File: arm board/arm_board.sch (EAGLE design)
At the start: 97 parts, among them IC1 OPAMP-DUALU, J1 APPPP45_PCB_HORIZ_RIGHT, J14 APPPP45_PCB_HORIZ_RIGHT, J15 APPPP45_PCB_HORIZ_RIGHT, J16 APPPP45_PCB_HORIZ_RIGHT, J17 APPPP45_PCB_HORIZ_RIGHT, J18 APPPP45_PCB_HORIZ_RIGHT, J19 ENCODER, J2 APPPP45_PCB_HORIZ_RIGHT, J20 ENCODER, J21 ENCODER, J22 ENCODER, J24 ENCODER, J3 APPPP45_PCB_HORIZ_RIGHT, Q1 Q_IRF7437SMD, U1 TIVA-1294, U3 MAX3232D

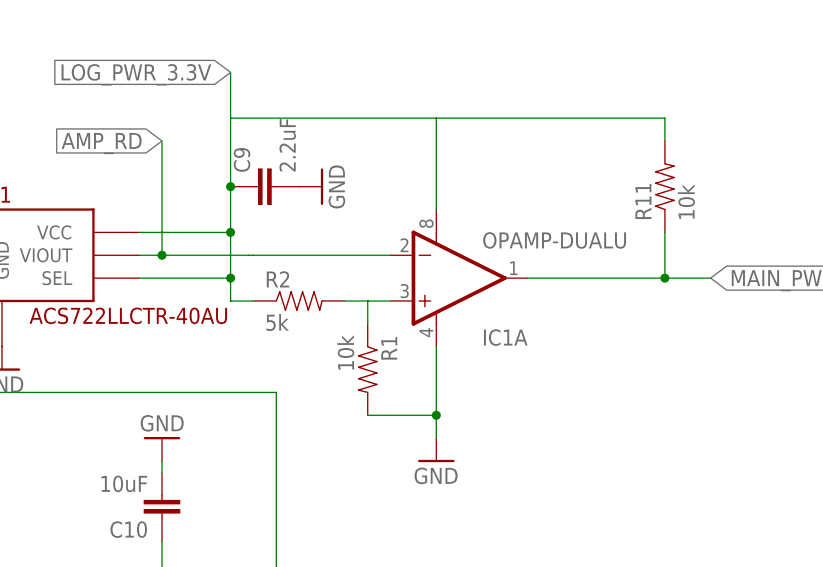
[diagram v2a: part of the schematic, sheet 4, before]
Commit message: Replaced opamp with one that actually exists
Turns out the one from sparkfun doesn't describe any model capable of
being found on digikey. wtf
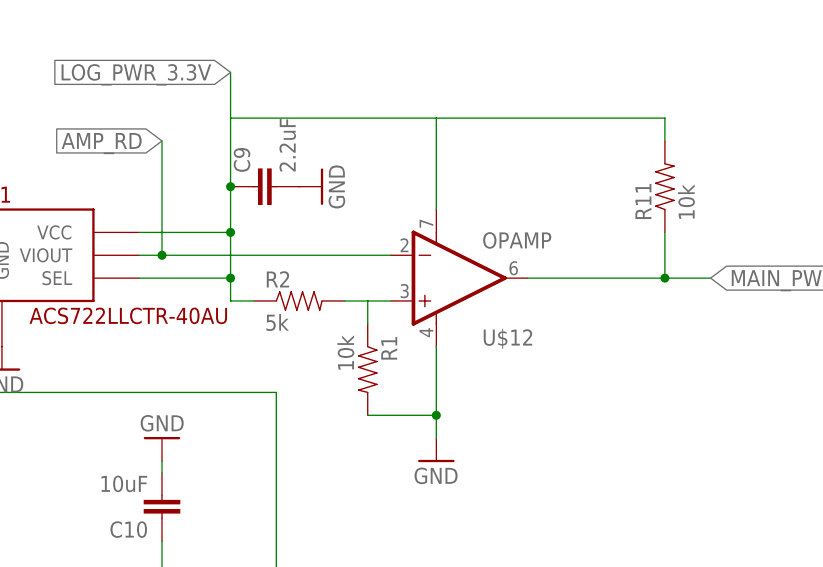
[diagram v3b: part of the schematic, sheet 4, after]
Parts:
- removed IC1: OPAMP-DUALU, SparkFun-AnalogIC:OPAMP-DUALU
- added U$12: OPAMP, MRDT-Semiconductors:OPAMP
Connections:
- net AMP_RD: now also U$12.-IN; no longer IC1A.-IN
- net GND: now also U$12.V-; no longer IC1A.V-
- net LOG_PWR_3.3V: now also U$12.V+; no longer IC1A.V+
- net MAIN_PWR_SWITCH_NFAULT: now also U$12.OUT; no longer IC1A.OUT
- net N$7: now also U$12.+IN; no longer IC1A.+IN
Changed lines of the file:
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@@
 <part name="C9" library="SparkFun-Capacitors" deviceset="0.1UF-25V(+80/-20%)(0603)" device="" value="2.2uF"/>
 <part name="GND24" library="SparkFun-Aesthetics" deviceset="GND" device=""/>
-<part name="IC1" library="SparkFun-AnalogIC" deviceset="OPAMP-DUAL" device="U"/>
 <part name="GND25" library="SparkFun-Aesthetics" deviceset="GND" device=""/>
 <part name="R1" library="SparkFun-Passives" deviceset="RESISTOR" device="0603-RES" value="10k"/>
@@
 <part name="D1" library="SparkFun-LED" deviceset="LED-YELLOW" device="LILYPAD" value="Yellow"/>
 <part name="R15" library="SparkFun-Resistors" deviceset="8.2K-5%" device="" value="3.3k"/>
+<part name="U$12" library="MRDT-Semiconductors" deviceset="OPAMP" device=""/>
 </parts>
 <sheets>
@@
 <instance part="C9" gate="G$1" x="33.02" y="-15.24" rot="R90"/>
 <instance part="GND24" gate="1" x="38.1" y="-15.24" rot="R90"/>
-<instance part="IC1" gate="A" x="50.8" y="-25.4"/>
 <instance part="GND25" gate="1" x="50.8" y="-45.72"/>
 <instance part="R1" gate="G$1" x="43.18" y="-35.56" rot="R270"/>
@@
 <instance part="GND30" gate="1" x="-129.54" y="-50.8" rot="R270"/>
 <instance part="FRAME4" gate="G$1" x="-210.82" y="-157.48"/>
+<instance part="U$12" gate="G$1" x="50.8" y="-25.4"/>
 </instances>
 <busses>
@@
 </segment>
 <segment>
-<pinref part="IC1" gate="A" pin="V-"/>
 <pinref part="GND25" gate="1" pin="GND"/>
 <wire x1="50.8" y1="-43.18" x2="50.8" y2="-40.64" width="0.1524" layer="91"/>
@@
 <wire x1="43.18" y1="-40.64" x2="50.8" y2="-40.64" width="0.1524" layer="91"/>
 <junction x="50.8" y="-40.64"/>
+<pinref part="U$12" gate="G$1" pin="V-"/>
 </segment>
 <segment>
@@
 <pinref part="C9" gate="G$1" pin="1"/>
 <junction x="27.94" y="-15.24"/>
-<pinref part="IC1" gate="A" pin="V+"/>
 <wire x1="27.94" y1="-25.4" x2="27.94" y2="-20.32" width="0.1524" layer="91"/>
 <wire x1="27.94" y1="-20.32" x2="27.94" y2="-15.24" width="0.1524" layer="91"/>
@@
 <wire x1="17.78" y1="-25.4" x2="27.94" y2="-25.4" width="0.1524" layer="91"/>
 <junction x="27.94" y="-25.4"/>
+<pinref part="U$12" gate="G$1" pin="V+"/>
 </segment>
 </net>
@@
 <junction x="20.32" y="-22.86"/>
 <label x="20.32" y="-10.16" size="1.778" layer="95" rot="R180" xref="yes"/>
-<pinref part="IC1" gate="A" pin="-IN"/>
-<wire x1="29.972" y1="-22.86" x2="30.48" y2="-22.86" width="0.1524" layer="91"/>
-<wire x1="30.48" y1="-22.86" x2="45.72" y2="-22.86" width="0.1524" layer="91"/>
-<wire x1="20.32" y1="-22.86" x2="29.972" y2="-22.86" width="0.1524" layer="91"/>
+<wire x1="20.32" y1="-22.86" x2="45.72" y2="-22.86" width="0.1524" layer="91"/>
+<pinref part="U$12" gate="G$1" pin="-IN"/>
 </segment>
 </net>
@@
 <segment>
 <pinref part="R2" gate="G$1" pin="2"/>
-<pinref part="IC1" gate="A" pin="+IN"/>
 <wire x1="40.64" y1="-27.94" x2="43.18" y2="-27.94" width="0.1524" layer="91"/>
 <pinref part="R1" gate="G$1" pin="1"/>
 <wire x1="43.18" y1="-27.94" x2="45.72" y2="-27.94" width="0.1524" layer="91"/>
 <wire x1="43.18" y1="-30.48" x2="43.18" y2="-27.94" width="0.1524" layer="91"/>
+<pinref part="U$12" gate="G$1" pin="+IN"/>
 </segment>
 </net>
 <net name="MAIN_PWR_SWITCH_NFAULT" class="0">
 <segment>
-<pinref part="IC1" gate="A" pin="OUT"/>
 <wire x1="60.96" y1="-25.4" x2="76.2" y2="-25.4" width="0.1524" layer="91"/>
 <label x="81.28" y="-25.4" size="1.778" layer="95" xref="yes"/>
@@
 <wire x1="76.2" y1="-20.32" x2="76.2" y2="-25.4" width="0.1524" layer="91"/>
 <junction x="76.2" y="-25.4"/>
-</segment>
-</net>
+<pinref part="U$12" gate="G$1" pin="OUT"/>
+</segment>
+</net>

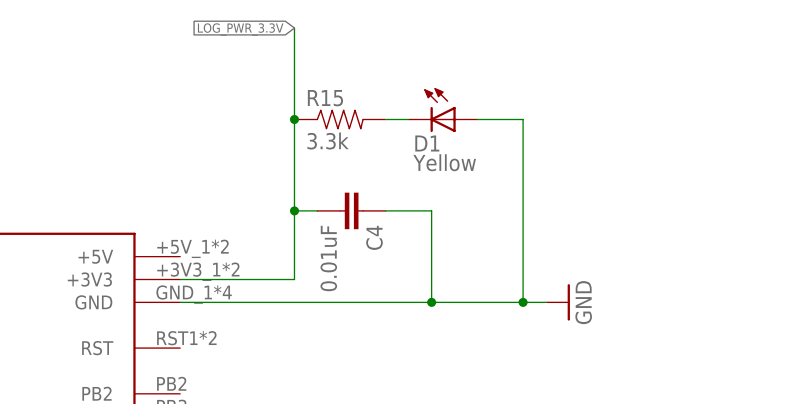
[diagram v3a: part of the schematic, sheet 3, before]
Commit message: I put the led on backwards. :-1:
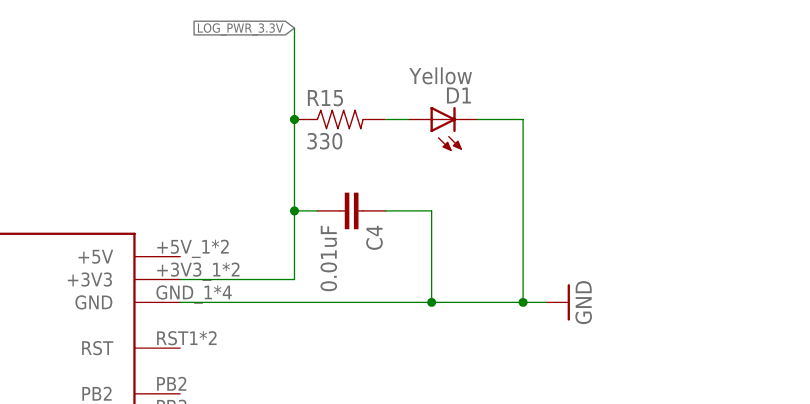
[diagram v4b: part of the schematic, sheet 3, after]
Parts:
- R15: value 3.3k -> 330
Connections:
- net GND: now also D1.C; no longer D1.A
- net N$16: now also D1.A; no longer D1.C
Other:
- moved on the sheet: D1
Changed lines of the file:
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@@
 <part name="FRAME4" library="frames" deviceset="A3L-LOC" device=""/>
 <part name="D1" library="SparkFun-LED" deviceset="LED-YELLOW" device="LILYPAD" value="Yellow"/>
-<part name="R15" library="SparkFun-Resistors" deviceset="8.2K-5%" device="" value="3.3k"/>
+<part name="R15" library="SparkFun-Resistors" deviceset="8.2K-5%" device="" value="330"/>
 <part name="U$12" library="MRDT-Semiconductors" deviceset="OPAMP" device=""/>
 </parts>
@@
 <instance part="GND15" gate="1" x="170.18" y="53.34"/>
 <instance part="FRAME3" gate="G$1" x="-99.06" y="-20.32"/>
-<instance part="D1" gate="G$1" x="53.34" y="137.16" rot="R270"/>
+<instance part="D1" gate="G$1" x="50.8" y="137.16" rot="R90"/>
 <instance part="R15" gate="G$1" x="40.64" y="137.16"/>
 </instances>
@@
 <wire x1="50.8" y1="127" x2="50.8" y2="116.84" width="0.1524" layer="91"/>
 <junction x="50.8" y="116.84"/>
-<pinref part="D1" gate="G$1" pin="A"/>
-<wire x1="55.88" y1="137.16" x2="60.96" y2="137.16" width="0.1524" layer="91"/>
 <wire x1="60.96" y1="137.16" x2="60.96" y2="116.84" width="0.1524" layer="91"/>
 <junction x="60.96" y="116.84"/>
+<pinref part="D1" gate="G$1" pin="C"/>
+<wire x1="55.88" y1="137.16" x2="60.96" y2="137.16" width="0.1524" layer="91"/>
 </segment>
 <segment>
@@
 <segment>
 <pinref part="R15" gate="G$1" pin="2"/>
-<pinref part="D1" gate="G$1" pin="C"/>
+<pinref part="D1" gate="G$1" pin="A"/>
 <wire x1="45.72" y1="137.16" x2="48.26" y2="137.16" width="0.1524" layer="91"/>
 </segment>

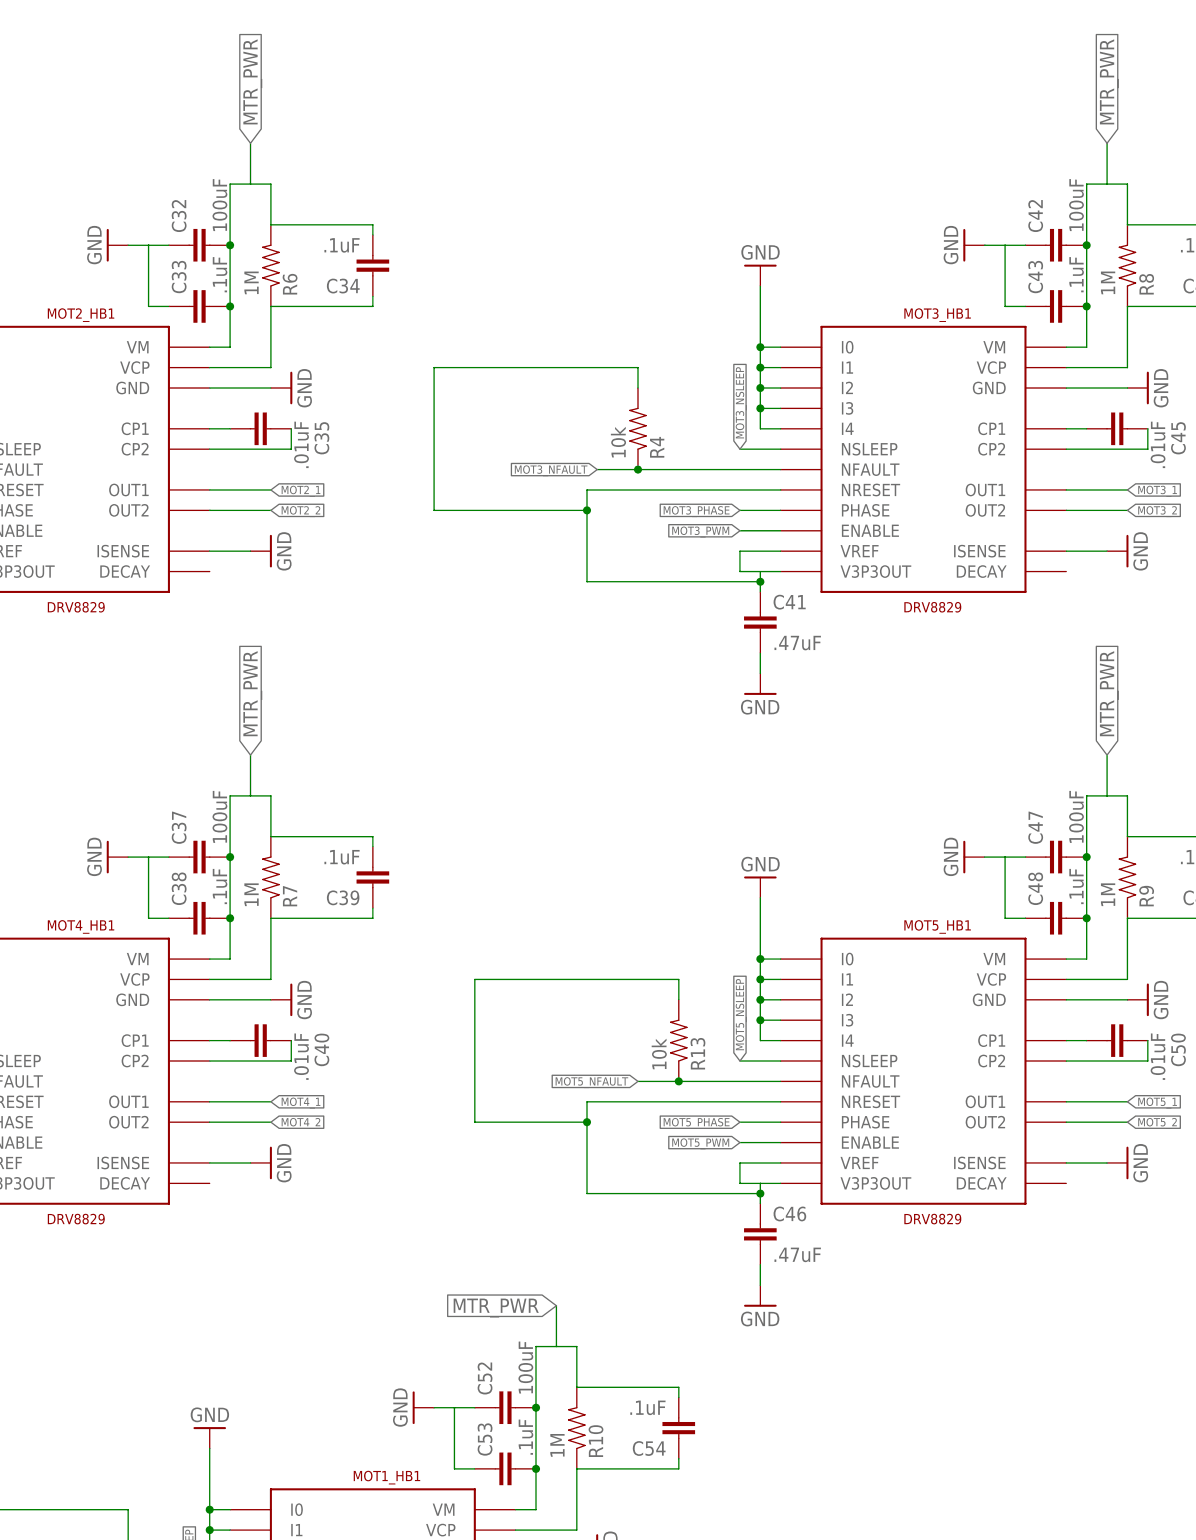
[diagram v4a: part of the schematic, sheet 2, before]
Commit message: Replaced 100uF 603 caps with 1210 caps
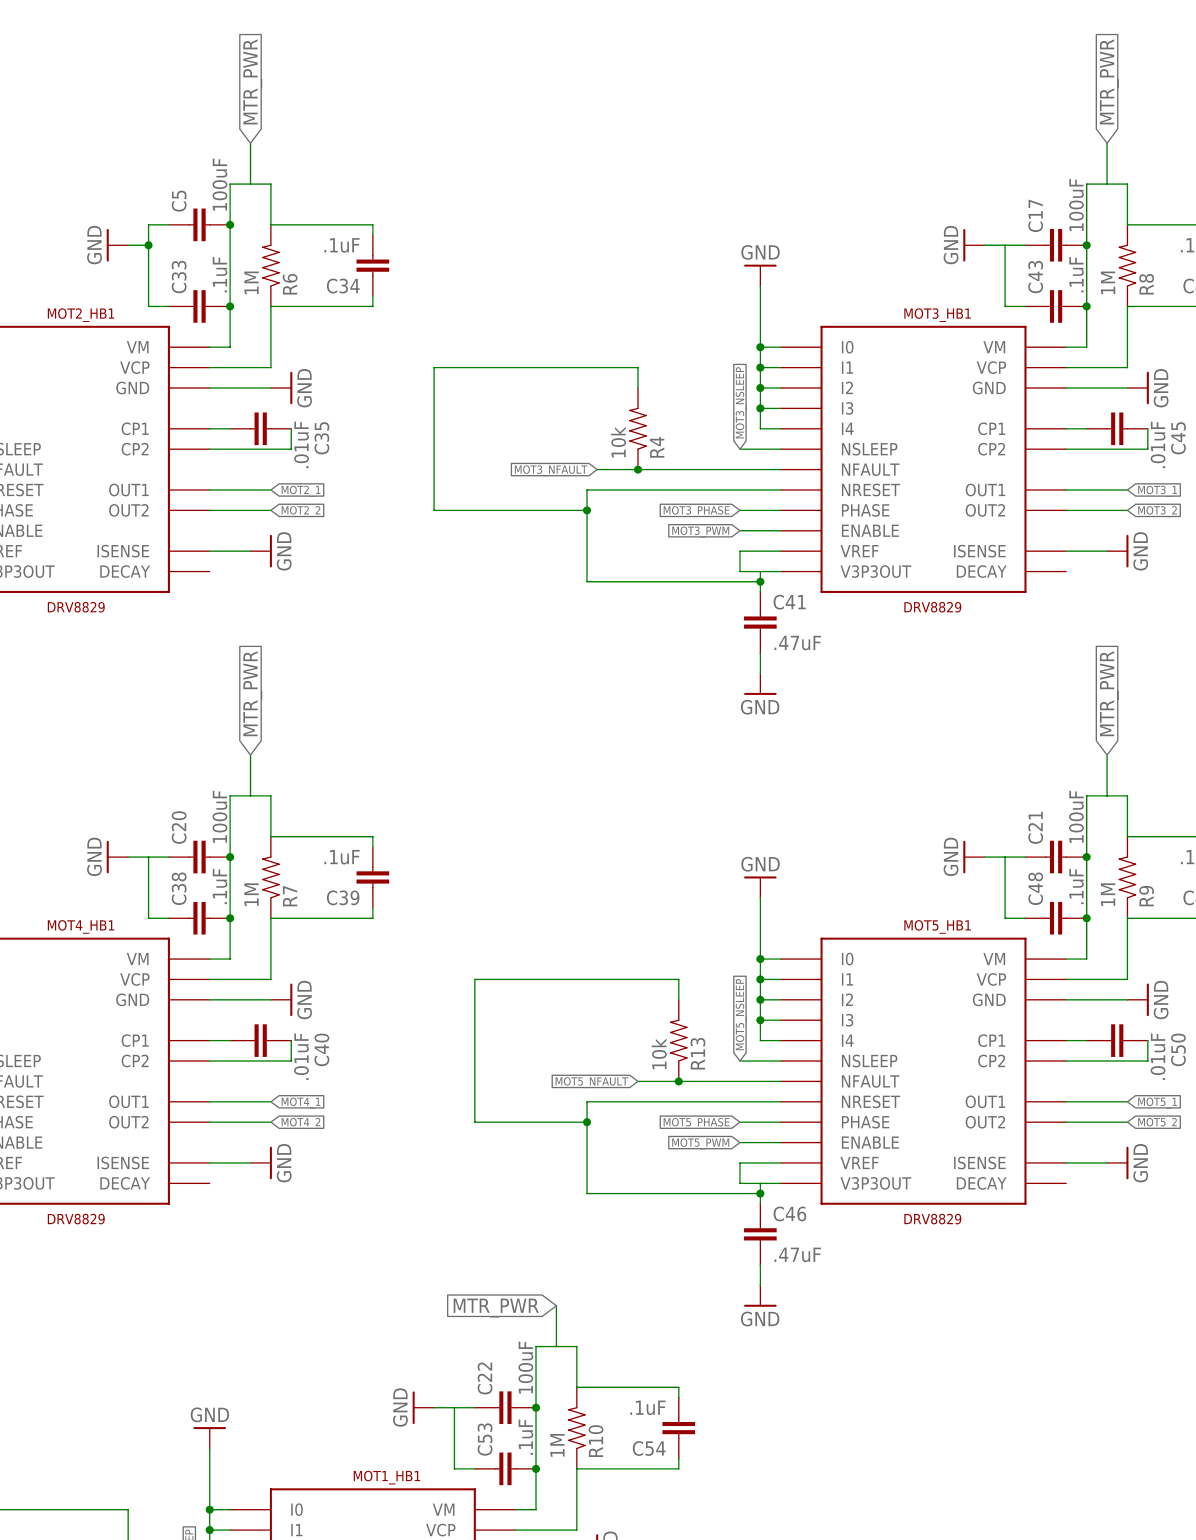
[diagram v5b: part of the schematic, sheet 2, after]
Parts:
- removed C32, C37, C42, C47, C52: 100uF, SparkFun-Capacitors:0.1UF-25V(+80/-20%)(0603)
- added C17, C20, C21, C22, C5: 100uF, SparkFun-Capacitors:CAP1210
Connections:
- net GND: now also C17.1, C20.1, C21.1, C22.1, C5.1; no longer C32.1, C37.1, C42.1, C47.1, C52.1
- net MTR_PWR: now also C17.2, C20.2, C21.2, C22.2, C5.2; no longer C32.2, C37.2, C42.2, C47.2, C52.2

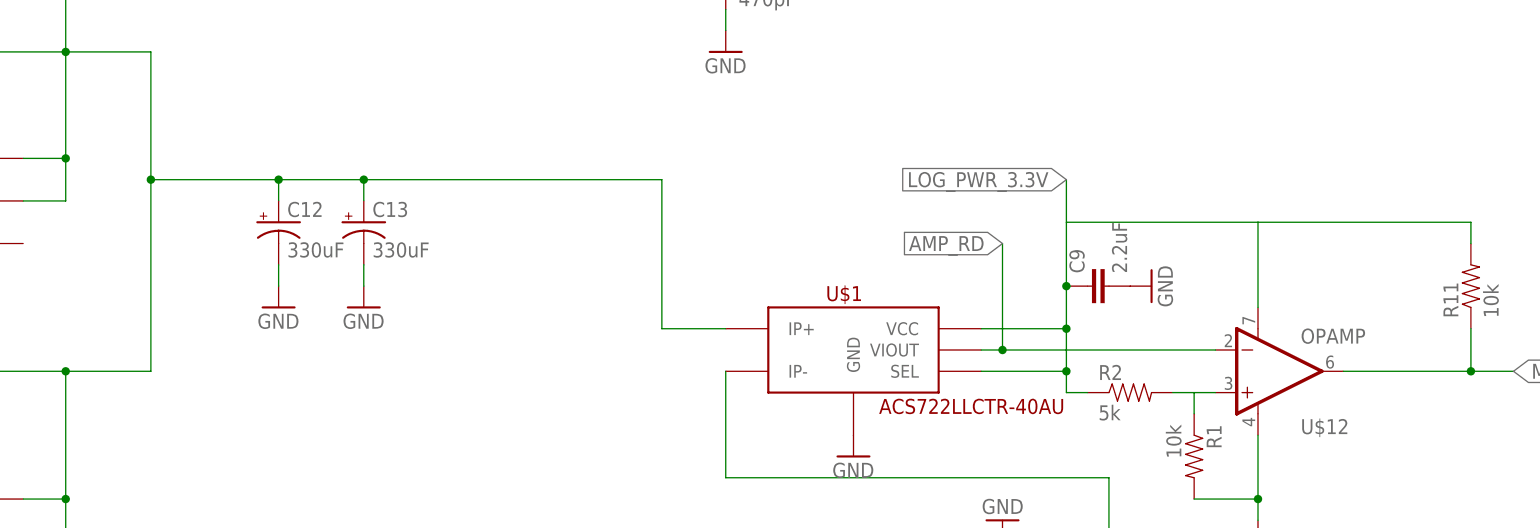
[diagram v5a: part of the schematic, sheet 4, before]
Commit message: Brought Schm in line with brd. Correct DRV8X issues
The schm wasn't uploaded with the brd the last few uploads, so now it's
back in line.

Changed some of the pins on the motor drivers from ground to 3.3V; turns
out those pins disable the chip if set to gnd or are left floating
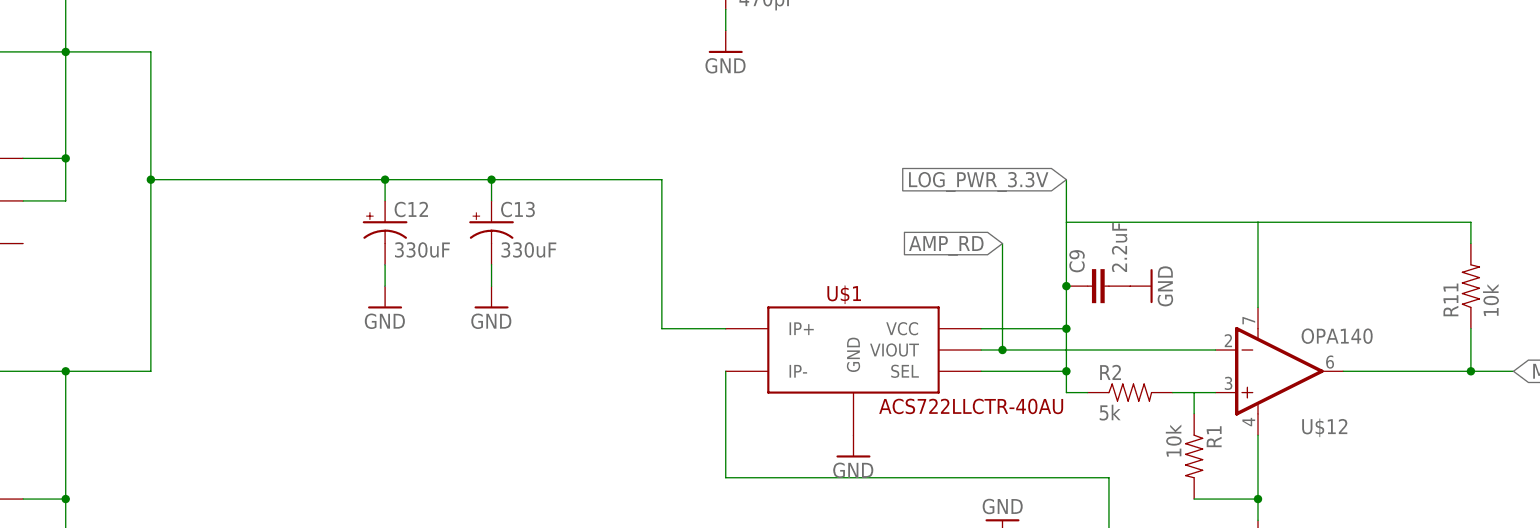
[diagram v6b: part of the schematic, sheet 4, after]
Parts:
- C12, C13: device SparkFun-Capacitors:CAP_POLC -> SparkFun-Capacitors:CAP_POLE
- U$12: value OPAMP -> OPA140; device MRDT-Semiconductors:OPAMP -> MRDT-Semiconductors:OPA140
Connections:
- net GND: no longer MOT1_HB1.I0, MOT1_HB1.I1, MOT1_HB1.I2, MOT1_HB1.I3, MOT1_HB1.I4, MOT2_HB1.I0, MOT2_HB1.I1, MOT2_HB1.I2, MOT2_HB1.I3, MOT2_HB1.I4, MOT3_HB1.I0, MOT3_HB1.I1, MOT3_HB1.I2, MOT3_HB1.I3, MOT3_HB1.I4, MOT4_HB1.I0, MOT4_HB1.I1, MOT4_HB1.I2, MOT4_HB1.I3, MOT4_HB1.I4, MOT5_HB1.I0, MOT5_HB1.I1, MOT5_HB1.I2, MOT5_HB1.I3, MOT5_HB1.I4
- net HB_3.3_OUTPUT5: now also MOT2_HB1.I0, MOT2_HB1.I1, MOT2_HB1.I2, MOT2_HB1.I3, MOT2_HB1.I4
- net HB_3.3_OUTPUT6: now also MOT4_HB1.I0, MOT4_HB1.I1, MOT4_HB1.I2, MOT4_HB1.I3, MOT4_HB1.I4
- net HB_3.3_OUTPUT7: now also MOT3_HB1.I0, MOT3_HB1.I1, MOT3_HB1.I2, MOT3_HB1.I3, MOT3_HB1.I4
- net HB_3.3_OUTPUT8: now also MOT5_HB1.I0, MOT5_HB1.I1, MOT5_HB1.I2, MOT5_HB1.I3, MOT5_HB1.I4
- net HB_3.3_OUTPUT9: now also MOT1_HB1.I0, MOT1_HB1.I1, MOT1_HB1.I2, MOT1_HB1.I3, MOT1_HB1.I4
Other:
- moved on the sheet: C12, C13
